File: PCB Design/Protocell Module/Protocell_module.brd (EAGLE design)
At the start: 100 x 80 mm, 7 parts, among them X1 RJ45-8X

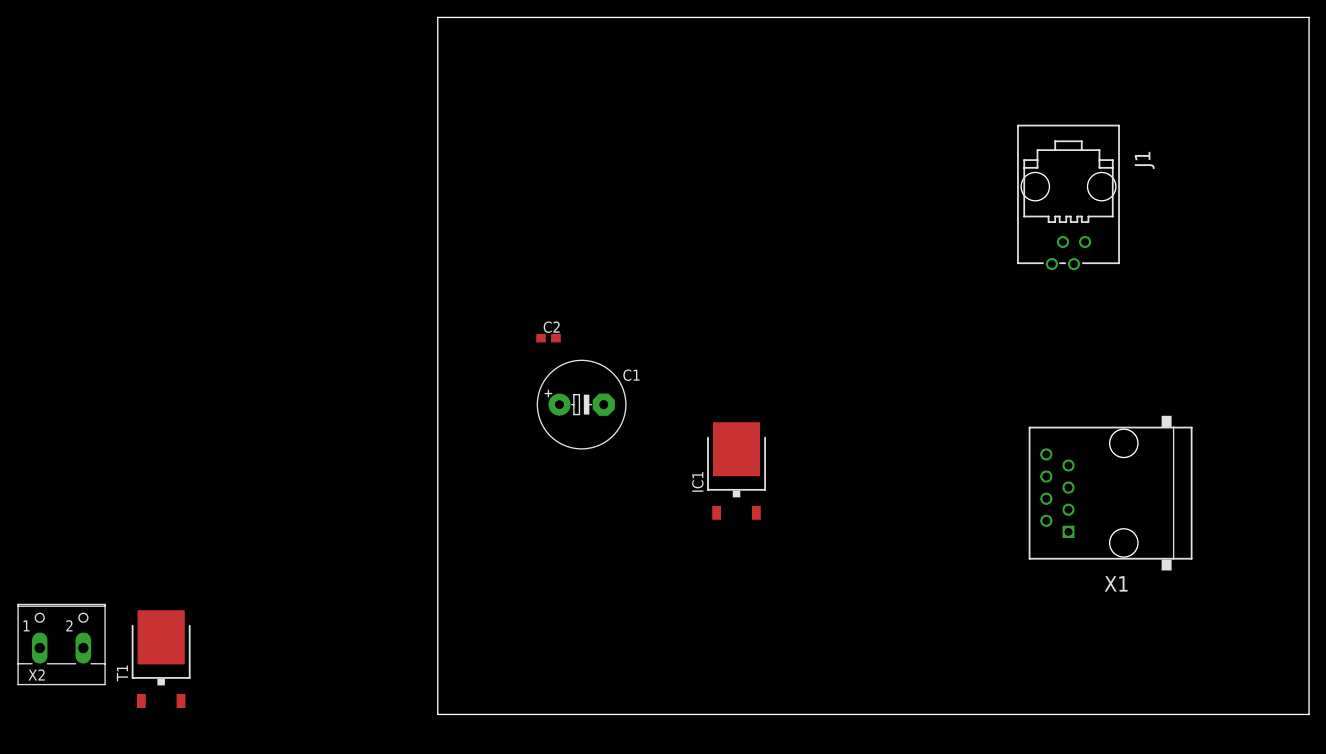
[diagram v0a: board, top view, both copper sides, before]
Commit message: Finished schematic and part placements
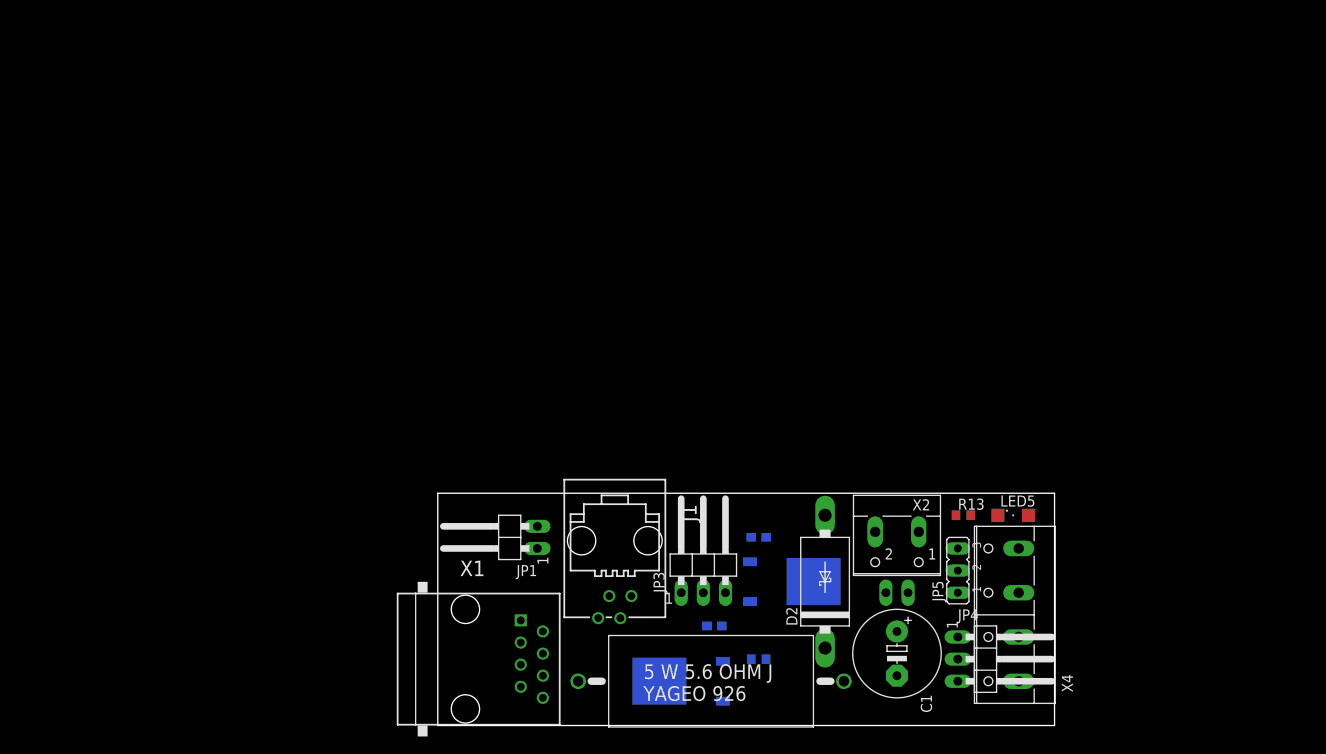
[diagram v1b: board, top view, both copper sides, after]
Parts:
- added C3: 1uF, rcl:C0603
- added D2: SB540E-G, CBLA_Test_bed_Library:DO201T15
- added JP1, JP2: (no value), CBLA_Test_bed_Library:1X02/90
- added JP3, JP4: (no value), CBLA_Test_bed_Library:1X03/90
- added JP5: (no value), jumper:JP2
- added LED5: (no value), led:SML1206
- added R1: 5.6, CBLA_Test_bed_Library:YAGEO_SQP500JB
- added R13: 470, CBLA_Test_bed_Library:R0603
- added R2: (no value), CBLA_Test_bed_Library:R0603
- added X4: (no value), con-wago-508:W237-4P
- IC1: value (none) -> MC7805BDTRKG; device CBLA_Test_bed_Library:DPACK -> CBLA_Test_bed_Library:DPACK_3
- moved X2 96.5 mm to (52.7, 19.7), turned to 180 degrees
- moved X1 77.9 mm to (3.17, 6.35), turned to 270 degrees
- moved J1 66.1 mm to (20.3, 19.1)
- moved T1 59.7 mm to (27.9, 3.81), flipped to the bottom, turned to 270 degrees
- moved C1 46.1 mm to (52.7, 6.99), turned to 270 degrees
- moved C2 33.2 mm to (36.8, 20.3), flipped to the bottom, turned to 180 degrees
- moved IC1 14.2 mm to (40.6, 15.2), flipped to the bottom, turned to 90 degrees
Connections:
- new net N$1: R1.1, T1.2
- new net N$10: LED5.C, R13.2
- new net N$3: JP2.2, R1.2, X2.2
- new net PWR_LED_GND: JP5.2, R13.1
- net +12V: now also D2.C, JP2.1, JP4.1, JP4.3, LED5.A, X2.1, X4.1, X4.4
- net +5V: now also J1.1, JP3.1; no longer J1.3
- net ANALOG1: now also C3.1, J1.3, JP1.2, JP3.3; no longer J1.1
- net GND: now also C3.2, D2.A, IC1.4, J1.2, JP3.2, JP4.2, JP5.1, R2.1, X4.2, X4.3; no longer IC1.2
- net PWM1: now also JP1.1, R2.2, T1.1
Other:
- board size 100 x 80 mm -> 70.8 x 26.7 mm

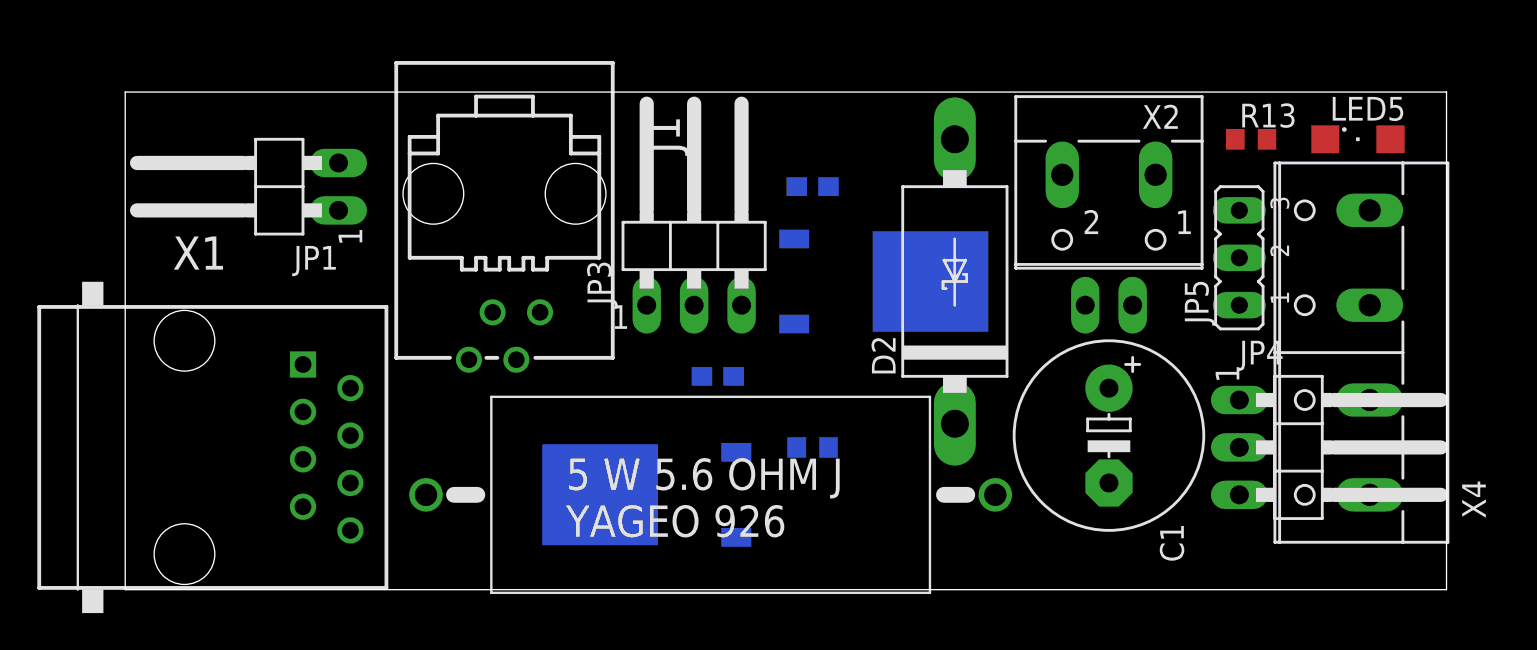
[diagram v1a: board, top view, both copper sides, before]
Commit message: Completed the Protocell Module PCB layout
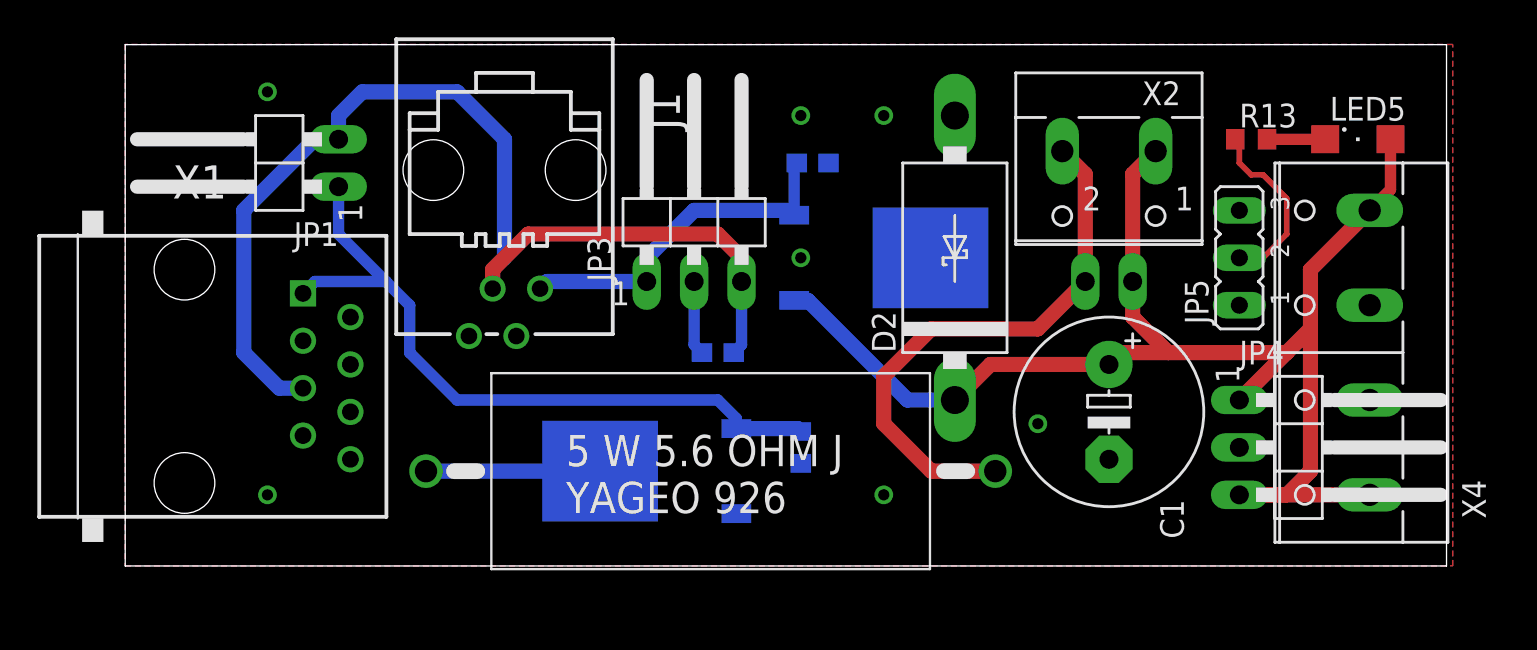
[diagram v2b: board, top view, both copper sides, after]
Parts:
- moved X1 3.81 mm to (3.17, 10.2)
- moved D2 1.27 mm to (44.5, 16.5)
- moved IC1 1.27 mm to (40.6, 16.5)
- moved C1 1.27 mm to (52.7, 8.26)
- moved R1 1.27 mm to (31.1, 5.08)
- moved T1 1.27 mm to (27.9, 5.08)
- moved C2 1.27 mm to (36.8, 21.6)
- moved C3 1.27 mm to (31.8, 11.4)
- moved J1 1.27 mm to (20.3, 20.3)
- moved JP1 1.27 mm to (7.62, 21.6)
- moved JP2 1.27 mm to (52.7, 19.1)
- moved JP3 1.27 mm to (30.5, 19.1)
- moved X2 1.27 mm to (52.7, 21.0)
- moved R2 0.63 mm to (36.2, 6.35), turned to 90 degrees
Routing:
- net +12V: track 0.00 -> 78.0 mm
- net ANALOG1: track 0.00 -> 59.2 mm
- net PWM1: track 0.00 -> 38.2 mm
- net N$3: track 0.00 -> 30.0 mm
- net +5V: track 0.00 -> 19.1 mm
- net PWR_LED_GND: track 0.00 -> 9.66 mm
- net N$1: track 0.00 -> 9.33 mm
- net GND: track 0.00 -> 3.98 mm, vias 0 -> 7
- net N$10: track 0.00 -> 3.12 mm
- added copper zone on layer 1, net GND
- added copper zone on layer 16, net GND
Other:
- board size 70.8 x 26.7 mm -> 70.8 x 27.9 mm

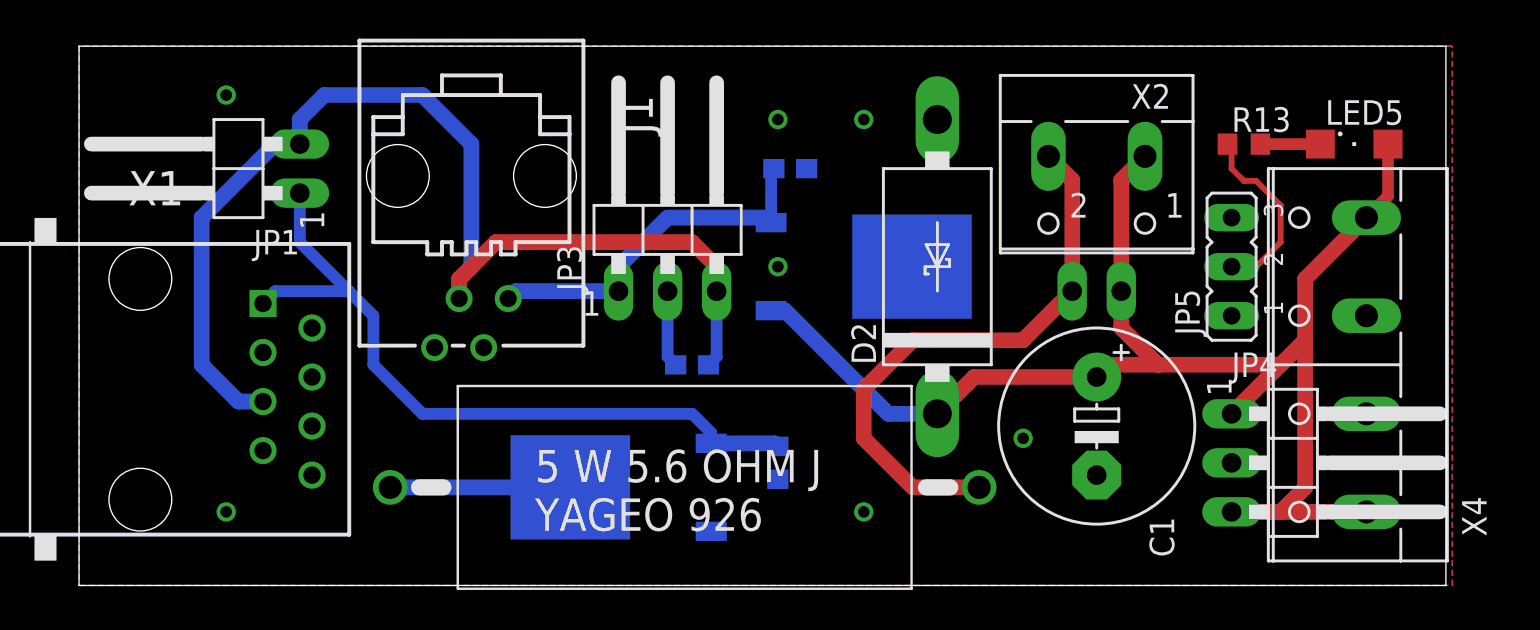
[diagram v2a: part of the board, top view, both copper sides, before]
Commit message: Polished silkscreen on protocell board
also add prefix to a part in library
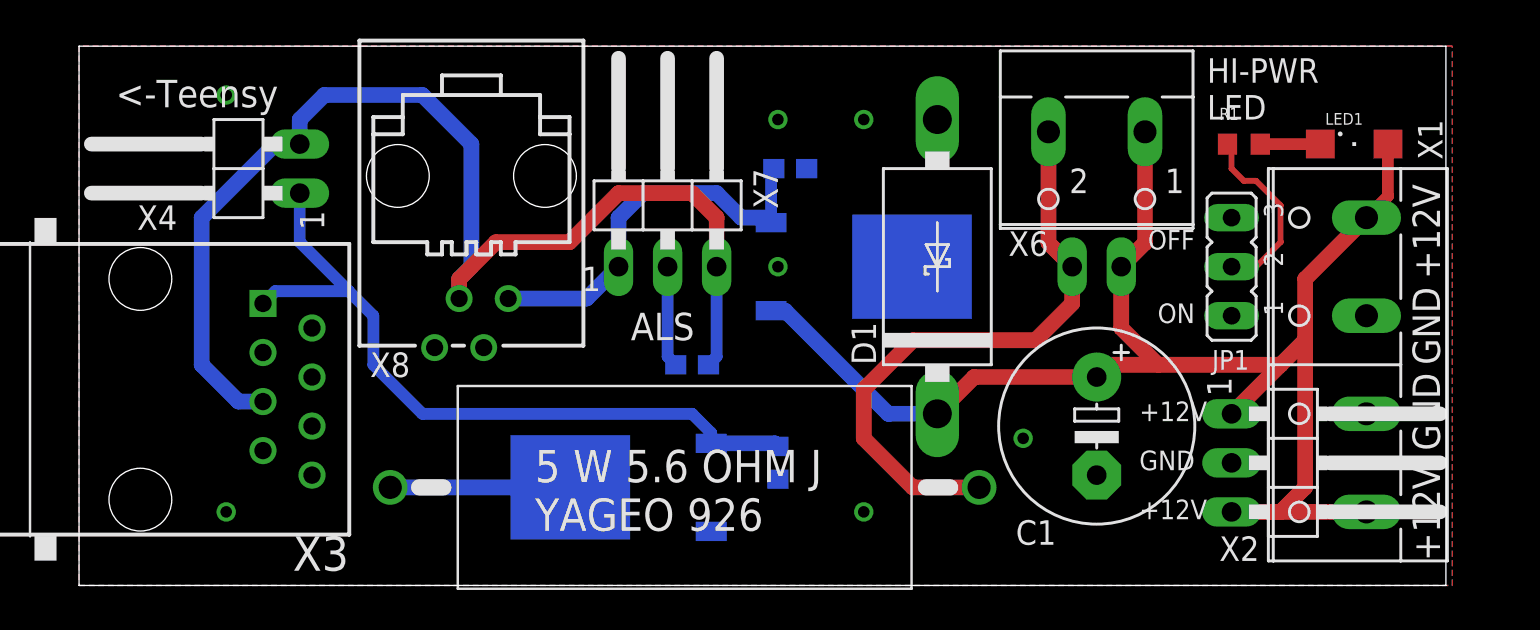
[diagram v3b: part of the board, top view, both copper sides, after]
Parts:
- removed JP2: (no value), CBLA_Test_bed_Library:1X02/90
- removed JP3, JP4: (no value), CBLA_Test_bed_Library:1X03/90
- removed JP5: (no value), jumper:JP2
- removed R13: 470, CBLA_Test_bed_Library:R0603
- added R3: 5.6, CBLA_Test_bed_Library:YAGEO_SQP500JB
- added X3: RJ45-8X, CBLA_Test_bed_Library:RJ45-NO-SHIELD
- added X5: (no value), CBLA_Test_bed_Library:1X02/90
- added X6: (no value), con-wago-500:W237-102
- added X7: (no value), CBLA_Test_bed_Library:1X03/90
- JP1: device CBLA_Test_bed_Library:1X02/90 -> jumper:JP2
- R1: value 5.6 -> 470; device CBLA_Test_bed_Library:YAGEO_SQP500JB -> CBLA_Test_bed_Library:R0603
- X1: value RJ45-8X -> (none); device CBLA_Test_bed_Library:RJ45-NO-SHIELD -> con-wago-508:W237-4P
- X2: device con-wago-500:W237-102 -> CBLA_Test_bed_Library:1X03/90
- X4: device con-wago-508:W237-4P -> CBLA_Test_bed_Library:1X02/90
- moved X1 62.9 mm to (66.0, 11.4), turned to 90 degrees
- moved X4 59.3 mm to (7.62, 21.6)
- moved JP1 52.3 mm to (59.7, 16.5)
- moved R1 34.2 mm to (60.3, 22.9)
- moved X2 18.2 mm to (63.5, 6.35), turned to 270 degrees
- renumbered D2 to D1, J1 to X8, LED5 to LED1
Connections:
- net +12V: now also X1.1, X1.4, X2.3, X5.1, X6.1; no longer JP2.1, JP4.1, JP4.3, X4.1, X4.4
- net +5V: now also X7.1; no longer JP3.1
- net ANALOG1: now also X3.5, X4.2, X7.3; no longer JP1.2, JP3.3, X1.5
- net GND: now also JP1.1, X1.2, X1.3, X2.2, X7.2; no longer JP3.2, JP4.2, JP5.1, X4.2, X4.3
- net N$1: now also R3.1; no longer R1.1
- net N$10: now also R1.2; no longer R13.2
- net N$3: now also R3.2, X5.2, X6.2; no longer JP2.2, R1.2, X2.2
- net PWM1: now also X3.1, X4.1; no longer JP1.1, X1.1
- net PWR_LED_GND: now also JP1.2, R1.1; no longer JP5.2, R13.1
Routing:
- net ANALOG1: track 59.2 -> 62.8 mm
- net +5V: track 19.1 -> 20.9 mm
- net N$3: track 30.0 -> 31.6 mm
- net GND: track 3.98 -> 5.25 mm
- net +12V: track 78.0 -> 79.3 mm
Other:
- board text added: "+12V"
- board text added: "<-Teensy"
- board text added: "ALS"
- board text added: "GND"
- board text added: "HI-PWR LED"
- board text added: "OFF"
- board text added: "ON"

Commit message: Added protocell module component to BOM
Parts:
- R2: value (none) -> 4.7k
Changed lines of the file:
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@@
 </element>
 <element name="R3" library="CBLA_Test_bed_Library" package="YAGEO_SQP500JB" value="5.6" x="31.115" y="5.08" smashed="yes"/>
-<element name="R2" library="CBLA_Test_bed_Library" package="R0603" value="" x="36.195" y="6.35" rot="MR90"/>
+<element name="R2" library="CBLA_Test_bed_Library" package="R0603" value="4.7k" x="36.195" y="6.35" rot="MR90"/>
 <element name="C3" library="rcl" package="C0603" value="1uF" x="31.75" y="11.43" smashed="yes" rot="MR0">
 <attribute name="NAME" x="32.385" y="12.065" size="1.27" layer="26" rot="MR0"/>
